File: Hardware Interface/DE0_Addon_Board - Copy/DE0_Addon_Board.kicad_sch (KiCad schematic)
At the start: 6 parts, among them J1 Conn_02x20_Odd_Even, J2 Conn_01x02_Male, J3 Conn_02x20_Odd_Even, U1 IS61WV25616EDBLL

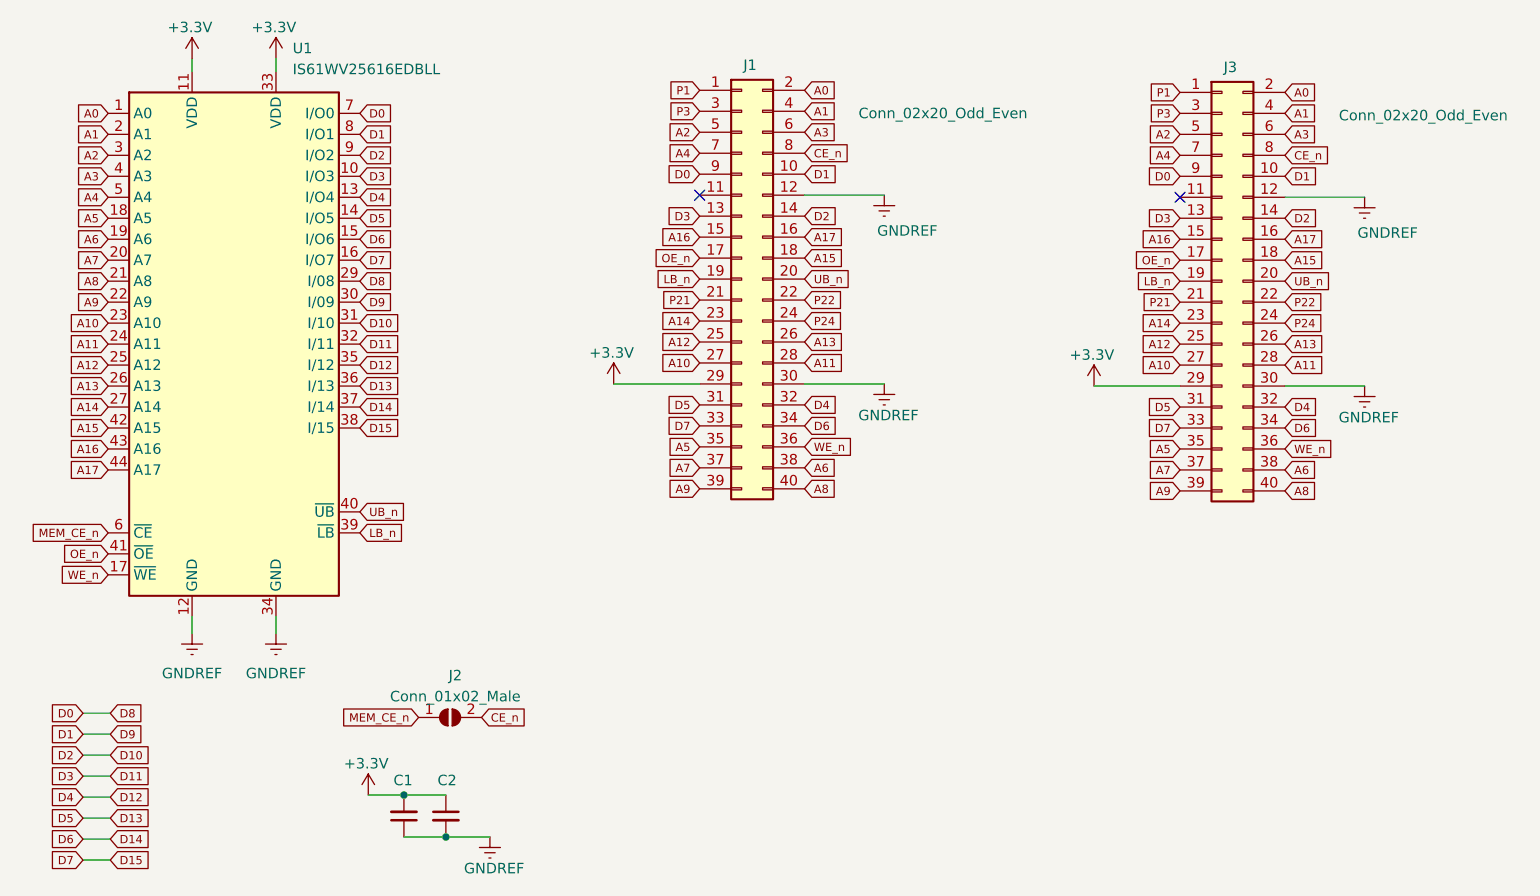
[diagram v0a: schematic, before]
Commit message: Added 2nd IDC connector in paralell with the SRAM
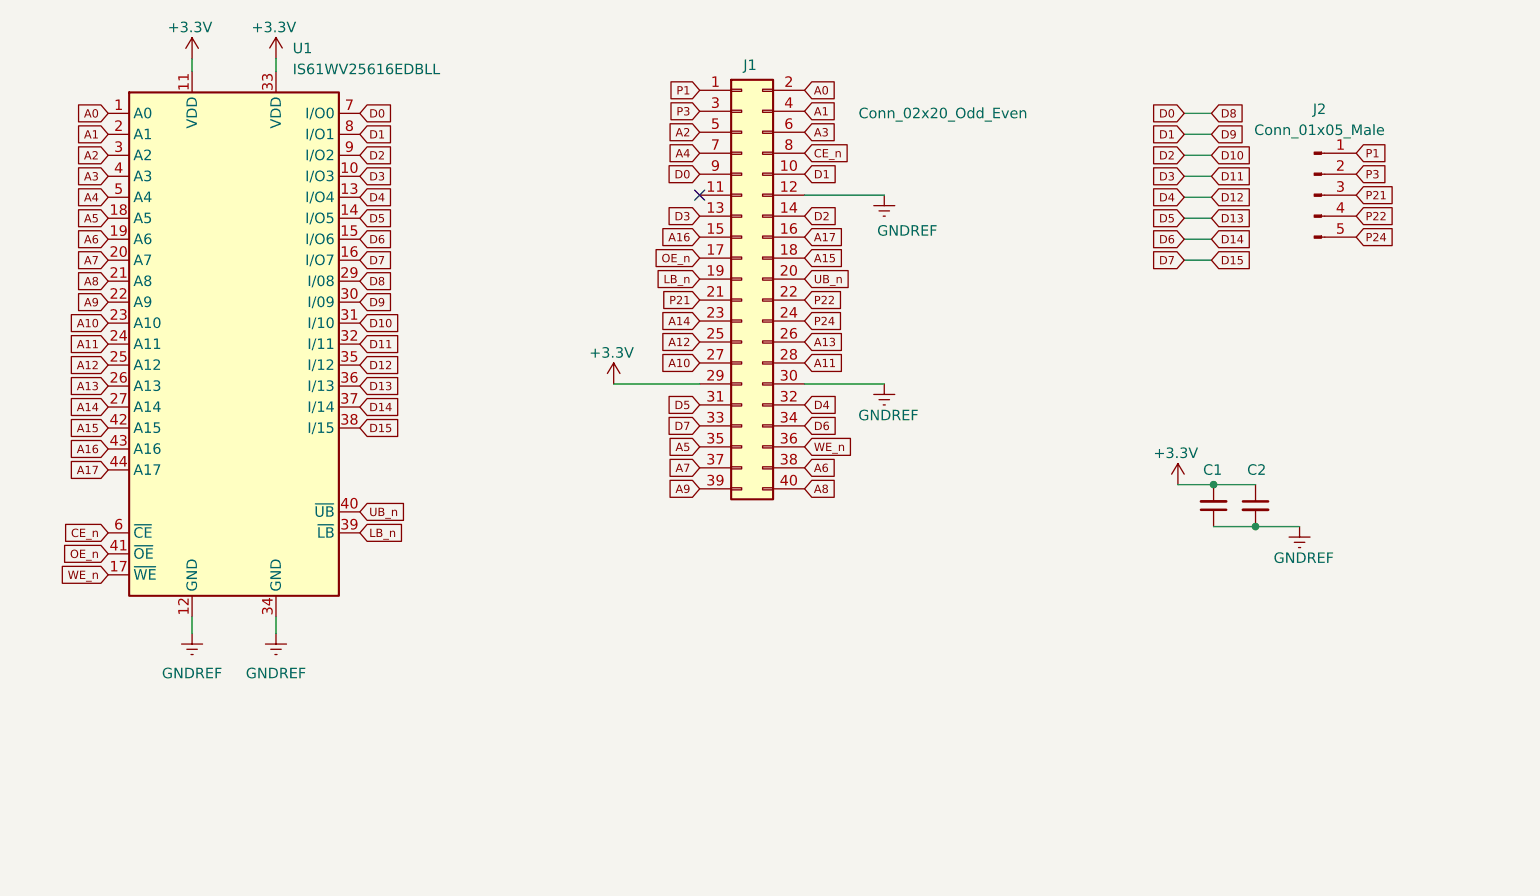
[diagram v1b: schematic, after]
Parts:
- removed J2: Conn_01x02_Male, Jumper:SolderJumper-2_P1.3mm_Open_Pad1.0x1.5mm, symbol Jumper:SolderJumper_2_Open
- removed J3: Conn_02x20_Odd_Even, Connector_PinHeader_2.54mm:PinHeader_2x20_P2.54mm_Vertical, symbol Connector_Generic:Conn_02x20_Odd_Even
- added J2: Conn_01x05_Male, Connector_PinHeader_2.54mm:PinHeader_1x05_P2.54mm_Vertical, symbol Connector:Conn_01x05_Male
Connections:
- net MEM_CE_n is gone; now on net CE_n: U1.6 (~{CE})
- net P1: now also J2.1 (Pin_1)
- net P21: now also J2.3 (Pin_3)
- net P22: now also J2.4 (Pin_4)
- net P24: now also J2.5 (Pin_5)
- net P3: now also J2.2 (Pin_2)
- no-connect marks 2 -> 1
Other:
- moved on the sheet: C1, C2
